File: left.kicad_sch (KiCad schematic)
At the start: 19 parts, among them K1 diode-choc, K10 diode-choc, K11 diode-choc, K12 diode-choc, K13 diode-choc, K14 diode-choc, K15 diode-choc, K16 diode-choc, K17 diode-choc, K18 diode-choc, K2 diode-choc, K3 diode-choc, K4 diode-choc, K5 diode-choc, K6 diode-choc, K7 diode-choc, K8 diode-choc, K9 diode-choc

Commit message: use narrower pinky spacing
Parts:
- K1, K11, K6: footprint pg1232:pg1232-DSSR -> pg1232:pg1232-DSSN
- K12, K2, K7: footprint pg1232:pg1232-DSS -> pg1232:pg1232-DSSR
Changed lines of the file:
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@@
       (effects (font (size 1.27 1.27)) (justify left) hide)
     )
-    (property "Footprint" "pg1232:pg1232-DSSR" (id 2) (at 62.23 22.86 0)
+    (property "Footprint" "pg1232:pg1232-DSSN" (id 2) (at 62.23 22.86 0)
       (effects (font (size 1.27 1.27)) hide)
     )
@@
       (effects (font (size 1.27 1.27)) (justify left) hide)
     )
-    (property "Footprint" "pg1232:pg1232-DSSR" (id 2) (at 62.23 34.29 0)
+    (property "Footprint" "pg1232:pg1232-DSSN" (id 2) (at 62.23 34.29 0)
       (effects (font (size 1.27 1.27)) hide)
     )
@@
       (effects (font (size 1.27 1.27)) (justify left) hide)
     )
-    (property "Footprint" "pg1232:pg1232-DSSR" (id 2) (at 62.23 45.72 0)
+    (property "Footprint" "pg1232:pg1232-DSSN" (id 2) (at 62.23 45.72 0)
       (effects (font (size 1.27 1.27)) hide)
     )
@@
       (effects (font (size 1.27 1.27)) (justify left) hide)
     )
-    (property "Footprint" "pg1232:pg1232-DSS" (id 2) (at 72.39 22.86 0)
+    (property "Footprint" "pg1232:pg1232-DSSR" (id 2) (at 72.39 22.86 0)
       (effects (font (size 1.27 1.27)) hide)
     )
@@
       (effects (font (size 1.27 1.27)) (justify left) hide)
     )
-    (property "Footprint" "pg1232:pg1232-DSS" (id 2) (at 72.39 34.29 0)
+    (property "Footprint" "pg1232:pg1232-DSSR" (id 2) (at 72.39 34.29 0)
       (effects (font (size 1.27 1.27)) hide)
     )
@@
       (effects (font (size 1.27 1.27)) (justify left) hide)
     )
-    (property "Footprint" "pg1232:pg1232-DSS" (id 2) (at 72.39 45.72 0)
+    (property "Footprint" "pg1232:pg1232-DSSR" (id 2) (at 72.39 45.72 0)
       (effects (font (size 1.27 1.27)) hide)
     )

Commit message: Hydrogen.PCB
- add Adafruit CAD files for Sharp display
- convert to all 3D printed mechanical parts
- update part dimensions to lowest estimate
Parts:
- BT1: footprint Connector_JST:JST_PH_S2B-PH-K_1x02_P2.00mm_Horizontal -> Connector_JST:JST_PH_S2B-PH-SM4-TB_1x02-1MP_P2.00mm_Horizontal; now left out of the parts list
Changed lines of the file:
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@@
   )
   (symbol (lib_id "Device:Battery_Cell") (at 40.64 50.8 0) (unit 1)
-    (in_bom yes) (on_board yes)
+    (in_bom no) (on_board yes)
     (property "Reference" "BT1" (id 0) (at 43.6372 48.3616 0)
       (effects (font (size 1.27 1.27)) (justify left))
@@
       (effects (font (size 1.27 1.27)) (justify left))
     )
-    (property "Footprint" "Connector_JST:JST_PH_S2B-PH-K_1x02_P2.00mm_Horizontal" (id 2) (at 40.64 49.276 90)
+    (property "Footprint" "Connector_JST:JST_PH_S2B-PH-SM4-TB_1x02-1MP_P2.00mm_Horizontal" (id 2) (at 40.64 49.276 90)
       (effects (font (size 1.27 1.27)) hide)
     )

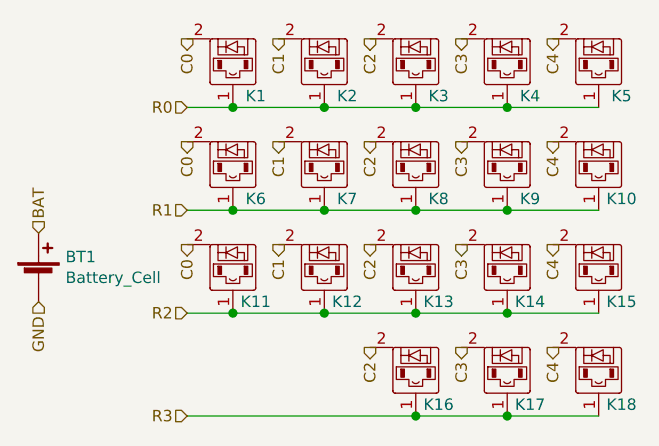
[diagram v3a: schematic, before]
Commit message: update PCB
use cirque trackpad, increase angle to 22.5
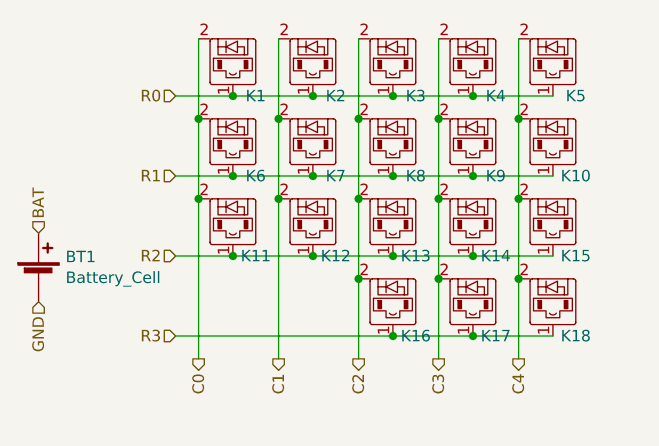
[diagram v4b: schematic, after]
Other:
- moved on the sheet: K1, K10, K11, K12, K13, K14, K15, K16, K17, K18, K2, K3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

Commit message: backup & remove useless things
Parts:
- removed BT1: Battery_Cell, Connector_JST:JST_PH_S2B-PH-SM4-TB_1x02-1MP_P2.00mm_Horizontal, symbol Device:Battery_Cell
- added C2: Li Cap, Capacitor_THT:CP_Radial_D13.0mm_P5.00mm, symbol Device:C_Polarized_US
- added C3: 4.7uF, Capacitor_SMD:C_0603_1608Metric, symbol Device:C
- added C4: 10nF, Capacitor_SMD:C_0603_1608Metric, symbol Device:C_Small
- added C6: 0.1uF, Capacitor_SMD:C_0603_1608Metric, symbol Device:C_Small
- added C7: 47uF, Capacitor_SMD:C_0805_2012Metric, symbol Device:C
- added H1: hinge-small, fusion:hinge1, symbol Mechanical:MountingHole
- added H2: hinge-big, fusion:hinge2, symbol Mechanical:MountingHole
- added H3, H4: mount-magnet, misc:m2-heat-insert-pad, symbol Mechanical:MountingHole
- added JP1: ~, Jumper:SolderJumper-2_P1.3mm_Open_RoundedPad1.0x1.5mm, symbol Jumper:SolderJumper_2_Open
- added JP2: SolderJumper_2_Open, Jumper:SolderJumper-2_P1.3mm_Open_RoundedPad1.0x1.5mm, symbol Jumper:SolderJumper_2_Open
- added L1: 22uH, Inductor_SMD:L_Wuerth_WE-TPC-3816, symbol Device:L
- added LCD1: adafruit-sharp-memory-display-no-useless, display:adafruit-sharp-memory-display-1.3in-no-mounting-no-useless, symbol display:adafruit-sharp-memory-display-no-useless
- added R1, R18: 4.12M, Resistor_SMD:R_0603_1608Metric, symbol Device:R_Small
- added R11, R15, R16, R6: 5.1M, Resistor_SMD:R_0603_1608Metric, symbol Device:R_Small
- added R17: 1M, Resistor_SMD:R_0603_1608Metric, symbol Device:R_Small
- added R19: 4.87M, Resistor_SMD:R_0603_1608Metric, symbol Device:R_Small
- added R2: 10M, Resistor_SMD:R_0603_1608Metric, symbol Device:R_Small
- added R4: 5.9M, Resistor_SMD:R_0603_1608Metric, symbol Device:R_Small
- added SC1: Solar_Cell, misc:KXOB25-05X3F, symbol Device:Solar_Cell
- added U6: ~, Package_DFN_QFN:QFN-16-1EP_3x3mm_P0.5mm_EP1.7x1.7mm, symbol Battery_Management:BQ25504
- added U7: MCP23S08, Package_SO:SOIC-18W_7.5x11.6mm_P1.27mm, symbol ic:MCP23S08
- K1, K11, K6: footprint pg1232:pg1232-DSSN -> pg1232:pg1232-DCN; symbol diode-choc:diode-choc -> switch:diode-choc
- K10, K15, K5: footprint pg1232:pg1232-DSSR -> pg1232:pg1232-DCN; symbol diode-choc:diode-choc -> switch:diode-choc
- K12, K2, K7: footprint pg1232:pg1232-DSSR -> pg1232:pg1232-DCR; symbol diode-choc:diode-choc -> switch:diode-choc
- K13, K16, K17, K18, K3, K8: footprint pg1232:pg1232-DSS -> pg1232:pg1232-DC; symbol diode-choc:diode-choc -> switch:diode-choc
- K14, K4, K9: footprint pg1232:pg1232-DSSL -> pg1232:pg1232-DCL; symbol diode-choc:diode-choc -> switch:diode-choc
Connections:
- net C1: now also U7.10 (GP0)
- net C2: now also U7.11 (GP1)
- net C3: now also U7.12 (GP2)
- net C4: now also U7.13 (GP3)
- net GND: now also C2.2, C3.1, C4.1, C6.1, C7.2, JP1.1 (A), JP2.1 (A), LCD1.4 (GND), R15.1, R18.1, R2.1, R6.1, SC1.2 (-), U6.1 (VSS), U6.12 (AVSS), U6.13 (VSS), U6.17 (PAD), U6.5 (OT_PROG), U7.4 (A1), U7.5 (A0), U7.9 (VSS)
- net R0: now also U7.14 (GP4)
- net R1: now also U7.15 (GP5)
- net R2: now also U7.16 (GP6)
- net R3: now also U7.17 (GP7)
- new net: L1.2, U6.16 (LBST)
- new net: R1.2, R4.2, U6.3 (VOC_SAMP)
- new net: JP1.2 (B), R17.1, R19.1, U6.9 (OK_HYST)
- new net: R15.2, R16.1, U6.8 (VBAT_UV)
- new net: R2.2, R4.1
- new net: JP2.2 (B), R18.2, R19.2, U6.10 (OK_PROG)
- new net: C4.2, U6.4 (VREF_SAMP)
- new net: R11.1, R6.2, U6.6 (VBAT_OV)
- new net: R11.2, R16.2, R17.2, U6.7 (VRDIV)
- new net 3V3: LCD1.5 (3V3), U7.18 (VDD), U7.6 (RESET)
- new net CAP: C2.1, U6.14 (VBAT)
- new net DISP_~{CS}: LCD1.1 (CS)
- new net IO_INT: U7.8 (INT)
- new net IO_~{CS}: U7.7 (CS)
- new net MISO: U7.3 (SO)
- new net MOSI: LCD1.2 (MOSI), U7.2 (SI)
- new net SCLK: LCD1.3 (SCK), U7.1 (SCK)
- new net SOLAR: C3.2, L1.1, R1.1, SC1.1 (+), U6.2 (VIN_DC)
- new net SOLAR_OUT: C6.2, C7.1, U6.15 (VSTOR)
- no-connect marks 0 -> 1
